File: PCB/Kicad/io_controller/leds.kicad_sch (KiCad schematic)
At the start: 36 parts, among them U1 74LS377, U2 74LS377

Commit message: io controller WIP ; simulated timer ; adjusted decoder ; adjusted LEDs
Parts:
- removed D10, D11, D12, D13, D14, D15, D16, D2, D3, D4, D5, D6, D7, D8, D9: LED, symbol Device:LED
- removed R10, R11, R12, R13, R14, R15, R16, R2, R3, R4, R5, R6, R7, R8, R9: 470, symbol Device:R
- added Dl10, Dl11, Dl12, Dl13, Dl14, Dl15, Dl16, Dl2, Dl3, Dl4, Dl5, Dl6, Dl7, Dl8, Dl9: red, LED_SMD:LED_0603_1608Metric, symbol Device:LED
- added Rl10, Rl11, Rl12, Rl13, Rl14, Rl15, Rl16, Rl2, Rl3, Rl4, Rl5, Rl6, Rl7, Rl8, Rl9: 680, Resistor_SMD:R_0402_1005Metric, symbol Device:R
- C1, C2: value 100nF -> 0.1u; footprint (none) -> Capacitor_SMD:C_0402_1005Metric
- Dl1: renamed from D1; value LED -> red; footprint (none) -> LED_SMD:LED_0603_1608Metric
- Rl1: renamed from R1; value 470 -> 680; footprint (none) -> Resistor_SMD:R_0402_1005Metric
- Ul1: renamed from U1; footprint (none) -> Package_SO:SOIC-20W_7.5x12.8mm_P1.27mm
- Ul2: renamed from U2; footprint (none) -> Package_SO:SOIC-20W_7.5x12.8mm_P1.27mm
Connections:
- net GND: now also Rl10.2, Rl11.2, Rl12.2, Rl13.2, Rl14.2, Rl15.2, Rl16.2, Rl2.2, Rl3.2, Rl4.2, Rl5.2, Rl6.2, Rl7.2, Rl8.2, Rl9.2
- net at Ul2.5 (Q1): now also Dl10.2 (A)
- net at Ul1.5 (Q1): now also Dl2.2 (A)
- net at Ul1.15 (Q5): now also Dl6.2 (A)
- net at Ul1.16 (Q6): now also Dl7.2 (A)
- net at Ul2.12 (Q4): now also Dl13.2 (A)
- net at Ul2.15 (Q5): now also Dl14.2 (A)
- net at Ul2.16 (Q6): now also Dl15.2 (A)
- net at Ul2.19 (Q7): now also Dl16.2 (A)
- net at Ul2.2 (Q0): now also Dl9.2 (A)
- net at Ul2.6 (Q2): now also Dl11.2 (A)
- net at Ul2.9 (Q3): now also Dl12.2 (A)
- net at Ul1.12 (Q4): now also Dl5.2 (A)
- net at Ul1.19 (Q7): now also Dl8.2 (A)
- net at Ul1.6 (Q2): now also Dl3.2 (A)
- net at Ul1.9 (Q3): now also Dl4.2 (A)
- new net: Dl6.1 (K), Rl6.1
- new net: Dl9.1 (K), Rl9.1
- new net: Dl2.1 (K), Rl2.1
- new net: Dl5.1 (K), Rl5.1
- new net: Dl11.1 (K), Rl11.1
- new net: Dl8.1 (K), Rl8.1
- new net: Dl3.1 (K), Rl3.1
- new net: Dl10.1 (K), Rl10.1
- new net: Dl7.1 (K), Rl7.1
- new net: Dl16.1 (K), Rl16.1
- new net: Dl4.1 (K), Rl4.1
- new net: Dl12.1 (K), Rl12.1
- new net: Dl14.1 (K), Rl14.1
- new net: Dl15.1 (K), Rl15.1
- new net: Dl13.1 (K), Rl13.1
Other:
- note added: "Dl1-Dl8"
- note added: "Dl9-Dl15"
- note added: "Rl1-Rl8"
- note added: "Rl9-Rl15"
- note added: "red"
- note added: "there is nothing that can go wrong here, fully excluded from simulation for performance reasons"
- note removed: "D1-D8"
- note removed: "D9-D15"
- note removed: "R1-R8"
- note removed: "R9-R15"

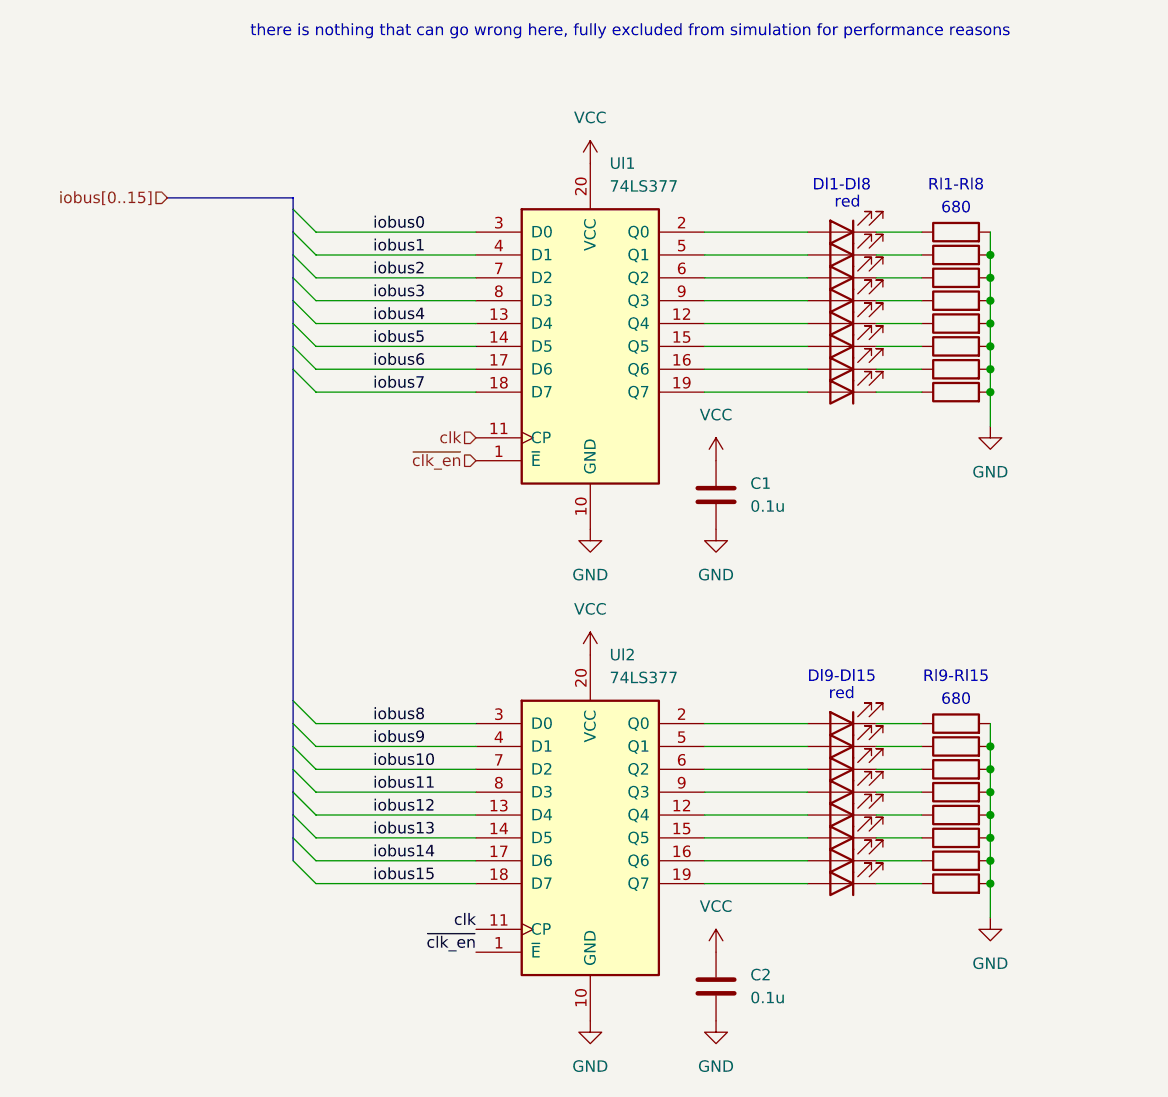
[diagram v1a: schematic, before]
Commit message: more spice models and bugfixes ; more tests of io_controller - mostly keyboard
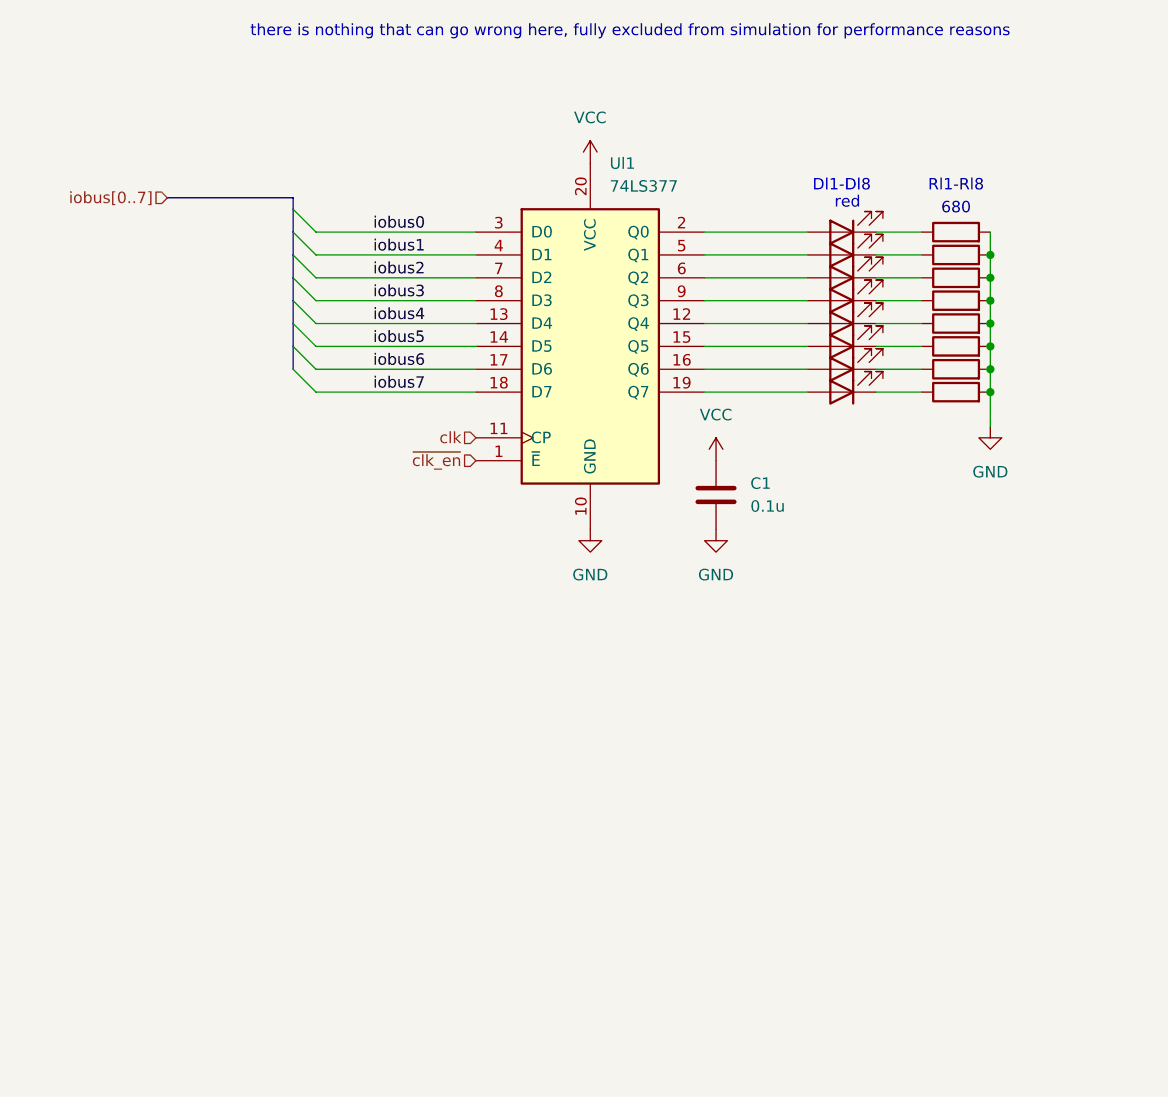
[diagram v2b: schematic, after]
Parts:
- removed C2: 0.1u, Capacitor_SMD:C_0402_1005Metric, symbol Device:C
- removed Dl10, Dl11, Dl12, Dl13, Dl14, Dl15, Dl16, Dl9: red, LED_SMD:LED_0603_1608Metric, symbol Device:LED
- removed Rl10, Rl11, Rl12, Rl13, Rl14, Rl15, Rl16, Rl9: 680, Resistor_SMD:R_0402_1005Metric, symbol Device:R
- removed Ul2: 74LS377, Package_SO:SOIC-20W_7.5x12.8mm_P1.27mm, symbol 74xx:74LS377
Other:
- note removed: "Dl9-Dl15"
- note removed: "Rl9-Rl15"
- company: (none) -> AGH Logic Unit
- title: (none) -> LED display
